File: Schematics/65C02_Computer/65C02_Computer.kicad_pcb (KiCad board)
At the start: 2 copper layers, 203.2 x 149.9 mm, 65 parts, among them J1 CLK Jumper, J10 LCD Connector, J2 Optional UART Port, J3 USB_B_Micro, J4 USB_B, J5 Power Connector, J6 Mini-DIN-6, J7 Expansion port, J8 VIA2PA, J9 VIA2PB, SW1 RESET, U1 74HC21, U10 ATtiny4313-PU, U11 65C22S, U12 65C22S, U2 74HC00, U3 74HC02, U4 NE555, U5 65C51N, U6 FT230XS, U7 65C02S, U8 28C256, U9 62256, X1 1MHz, X2 1.8432MHz

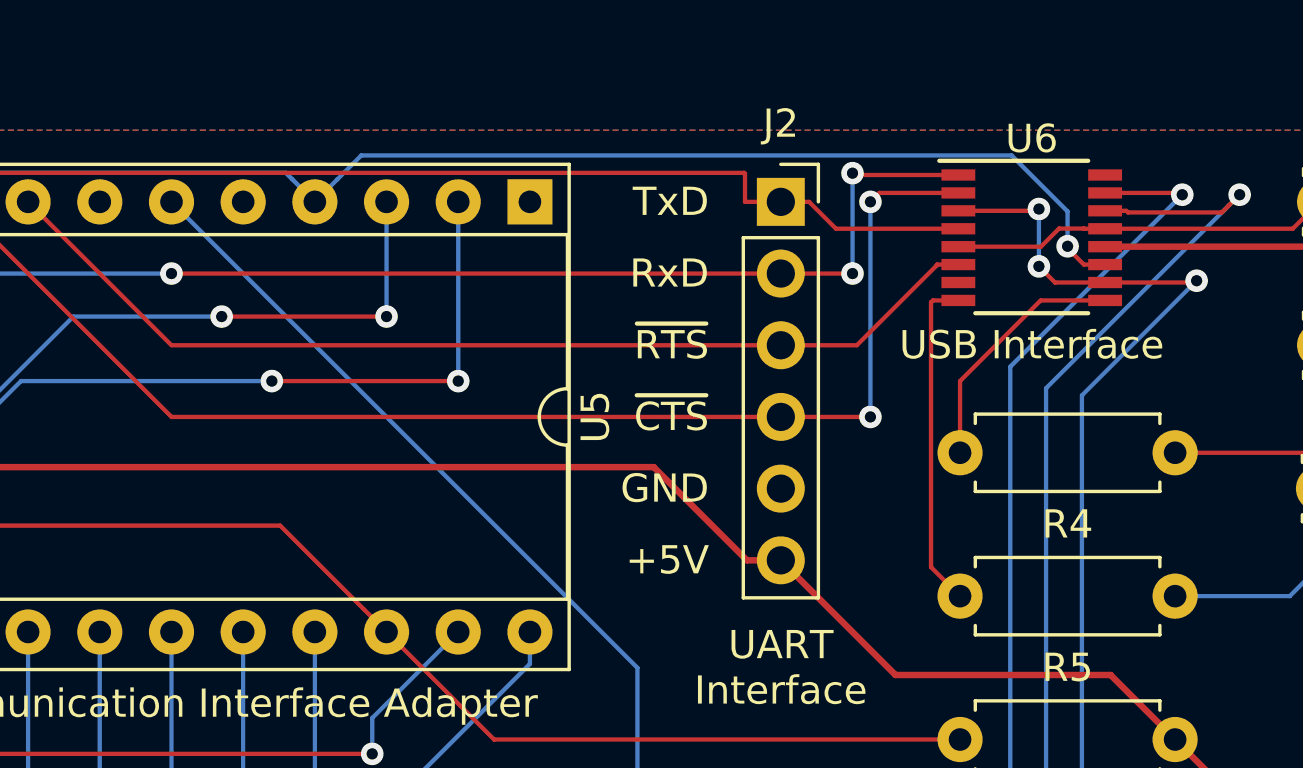
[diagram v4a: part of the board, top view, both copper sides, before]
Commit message: PCB RC4 - added longer pads to SSOP chip
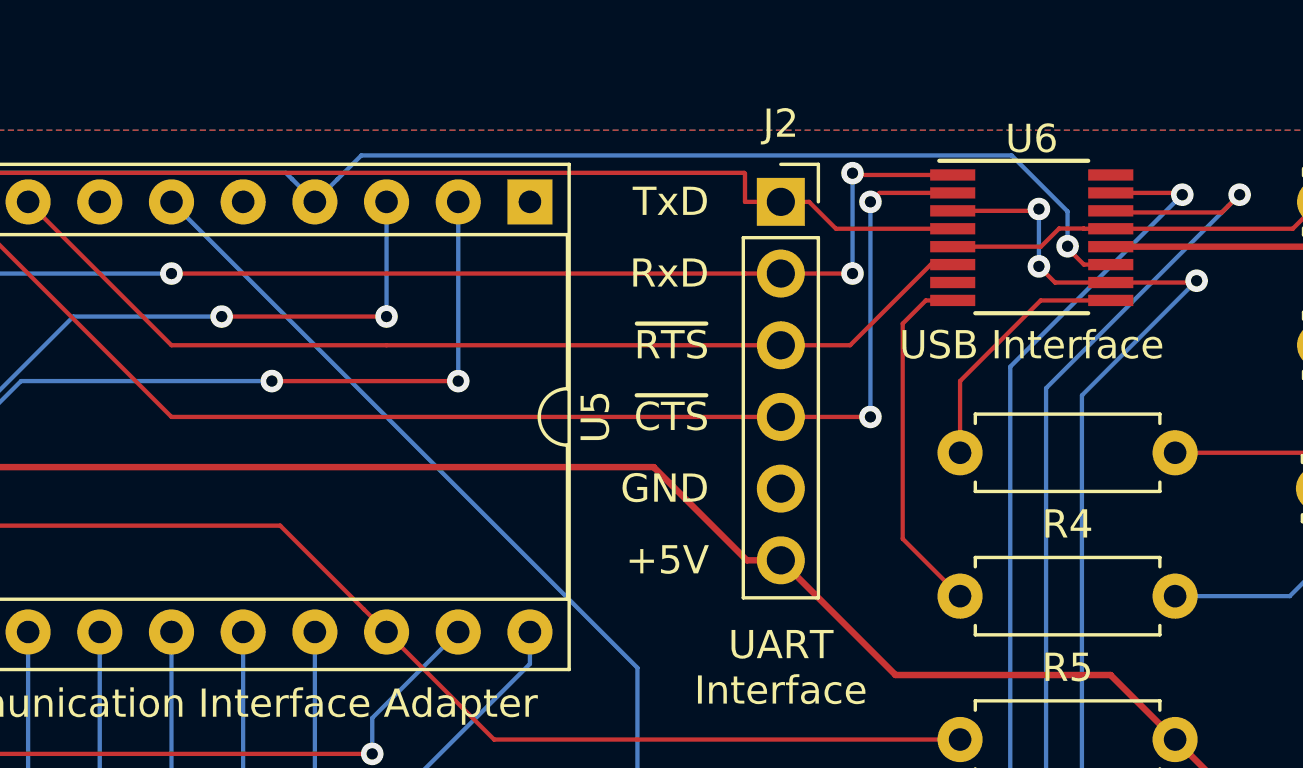
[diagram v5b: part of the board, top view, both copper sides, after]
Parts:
- U6: footprint Package_SO:SSOP-16_3.9x4.9mm_P0.635mm -> 65C02_Computer:SSOP-16_3.9x4.9mm_P0.635mm_long_pads
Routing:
- net USBD+: track 11.9 -> 12.6 mm
- net ~RTS: track 36.3 -> 36.8 mm
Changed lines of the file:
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@@
-(kicad_pcb (version 20171130) (host pcbnew "(5.1.5)-3")
+(kicad_pcb (version 20171130) (host pcbnew "(5.1.5-0-10_14)")
   (general
     (thickness 1.6)
     (drawings 126)
-    (tracks 1583)
+    (tracks 1585)
     (zones 0)
     (modules 65)
@@
     (0 F.Cu signal)
     (31 B.Cu signal)
-    (32 B.Adhes user)
-    (33 F.Adhes user)
-    (34 B.Paste user)
-    (35 F.Paste user)
+    (32 B.Adhes user hide)
+    (33 F.Adhes user hide)
+    (34 B.Paste user hide)
+    (35 F.Paste user hide)
     (36 B.SilkS user)
     (37 F.SilkS user)
     (38 B.Mask user)
     (39 F.Mask user)
-    (40 Dwgs.User user)
-    (41 Cmts.User user)
-    (42 Eco1.User user)
-    (43 Eco2.User user)
+    (40 Dwgs.User user hide)
+    (41 Cmts.User user hide)
+    (42 Eco1.User user hide)
+    (43 Eco2.User user hide)
     (44 Edge.Cuts user)
-    (45 Margin user)
-    (46 B.CrtYd user)
-    (47 F.CrtYd user)
+    (45 Margin user hide)
+    (46 B.CrtYd user hide)
+    (47 F.CrtYd user hide)
     (48 B.Fab user hide)
     (49 F.Fab user hide)
@@
       (psa4output false)
       (plotreference true)
-      (plotvalue true)
+      (plotvalue false)
       (plotinvisibletext false)
       (padsonsilk false)
@@
     (add_net +5V)
   )
-  (module Package_SO:SSOP-16_3.9x4.9mm_P0.635mm (layer F.Cu)
+  (module 65C02_Computer:SSOP-16_3.9x4.9mm_P0.635mm_long_pads (layer F.Cu)
     (at 189.23 29.21)
     (descr "SSOP16: plastic shrink small outline package; 16 leads; body width 3.9 mm; lead pitch 0.635; (see NXP SSOP-TSSOP-VSO-REFLOW.pdf and sot519-1_po.pdf)")
@@
     (fp_line (start -3.275 -2.725) (end 2 -2.725) (layer F.SilkS) (width 0.15))
     (fp_line (start -2 2.675) (end 2 2.675) (layer F.SilkS) (width 0.15))
-    (fp_line (start -3.45 2.8) (end 3.45 2.8) (layer F.CrtYd) (width 0.05))
-    (fp_line (start -3.45 -2.85) (end 3.45 -2.85) (layer F.CrtYd) (width 0.05))
-    (fp_line (start 3.45 -2.85) (end 3.45 2.8) (layer F.CrtYd) (width 0.05))
-    (fp_line (start -3.45 -2.85) (end -3.45 2.8) (layer F.CrtYd) (width 0.05))
+    (fp_line (start -3.65 2.8) (end 3.65 2.8) (layer F.CrtYd) (width 0.05))
+    (fp_line (start -3.65 -2.85) (end 3.65 -2.85) (layer F.CrtYd) (width 0.05))
+    (fp_line (start 3.65 -2.85) (end 3.65 2.8) (layer F.CrtYd) (width 0.05))
+    (fp_line (start -3.65 -2.85) (end -3.65 2.8) (layer F.CrtYd) (width 0.05))
     (fp_line (start -1.95 -1.45) (end -0.95 -2.45) (layer F.Fab) (width 0.15))
     (fp_line (start -1.95 2.45) (end -1.95 -1.45) (layer F.Fab) (width 0.15))
@@
     (fp_line (start 1.95 -2.45) (end 1.95 2.45) (layer F.Fab) (width 0.15))
     (fp_line (start -0.95 -2.45) (end 1.95 -2.45) (layer F.Fab) (width 0.15))
-    (pad 16 smd rect (at 2.6 -2.2225) (size 1.2 0.4) (layers F.Cu F.Paste F.Mask)
+    (pad 16 smd rect (at 2.8 -2.2225) (size 1.6 0.4) (layers F.Cu F.Paste F.Mask)
       (net 105 "Net-(U6-Pad16)"))
-    (pad 15 smd rect (at 2.6 -1.5875) (size 1.2 0.4) (layers F.Cu F.Paste F.Mask)
+    (pad 15 smd rect (at 2.8 -1.5875) (size 1.6 0.4) (layers F.Cu F.Paste F.Mask)
       (net 4 "Net-(D2-Pad1)"))
-    (pad 14 smd rect (at 2.6 -0.9525) (size 1.2 0.4) (layers F.Cu F.Paste F.Mask)
+    (pad 14 smd rect (at 2.8 -0.9525) (size 1.6 0.4) (layers F.Cu F.Paste F.Mask)
       (net 7 "Net-(D3-Pad1)"))
-    (pad 13 smd rect (at 2.6 -0.3175) (size 1.2 0.4) (layers F.Cu F.Paste F.Mask)
+    (pad 13 smd rect (at 2.8 -0.3175) (size 1.6 0.4) (layers F.Cu F.Paste F.Mask)
       (net 2 GND))
-    (pad 12 smd rect (at 2.6 0.3175) (size 1.2 0.4) (layers F.Cu F.Paste F.Mask)
+    (pad 12 smd rect (at 2.8 0.3175) (size 1.6 0.4) (layers F.Cu F.Paste F.Mask)
       (net 1 +5V))
-    (pad 11 smd rect (at 2.6 0.9525) (size 1.2 0.4) (layers F.Cu F.Paste F.Mask)
+    (pad 11 smd rect (at 2.8 0.9525) (size 1.6 0.4) (layers F.Cu F.Paste F.Mask)
       (net 37 ~RES))
-    (pad 10 smd rect (at 2.6 1.5875) (size 1.2 0.4) (layers F.Cu F.Paste F.Mask)
+    (pad 10 smd rect (at 2.8 1.5875) (size 1.6 0.4) (layers F.Cu F.Paste F.Mask)
       (net 72 "Net-(R10-Pad1)"))
-    (pad 9 smd rect (at 2.6 2.2225) (size 1.2 0.4) (layers F.Cu F.Paste F.Mask)
+    (pad 9 smd rect (at 2.8 2.2225) (size 1.6 0.4) (layers F.Cu F.Paste F.Mask)
       (net 71 USBD-))
-    (pad 8 smd rect (at -2.6 2.2225) (size 1.2 0.4) (layers F.Cu F.Paste F.Mask)
+    (pad 8 smd rect (at -2.8 2.2225) (size 1.6 0.4) (layers F.Cu F.Paste F.Mask)
       (net 70 USBD+))
-    (pad 7 smd rect (at -2.6 1.5875) (size 1.2 0.4) (layers F.Cu F.Paste F.Mask)
+    (pad 7 smd rect (at -2.8 1.5875) (size 1.6 0.4) (layers F.Cu F.Paste F.Mask)
       (net 106 "Net-(U6-Pad7)"))
-    (pad 6 smd rect (at -2.6 0.9525) (size 1.2 0.4) (layers F.Cu F.Paste F.Mask)
+    (pad 6 smd rect (at -2.8 0.9525) (size 1.6 0.4) (layers F.Cu F.Paste F.Mask)
       (net 93 ~RTS))
-    (pad 5 smd rect (at -2.6 0.3175) (size 1.2 0.4) (layers F.Cu F.Paste F.Mask)
+    (pad 5 smd rect (at -2.8 0.3175) (size 1.6 0.4) (layers F.Cu F.Paste F.Mask)
       (net 2 GND))
-    (pad 4 smd rect (at -2.6 -0.3175) (size 1.2 0.4) (layers F.Cu F.Paste F.Mask)
+    (pad 4 smd rect (at -2.8 -0.3175) (size 1.6 0.4) (layers F.Cu F.Paste F.Mask)
       (net 92 TxD))
-    (pad 3 smd rect (at -2.6 -0.9525) (size 1.2 0.4) (layers F.Cu F.Paste F.Mask)
+    (pad 3 smd rect (at -2.8 -0.9525) (size 1.6 0.4) (layers F.Cu F.Paste F.Mask)
       (net 72 "Net-(R10-Pad1)"))
-    (pad 2 smd rect (at -2.6 -1.5875) (size 1.2 0.4) (layers F.Cu F.Paste F.Mask)
+    (pad 2 smd rect (at -2.8 -1.5875) (size 1.6 0.4) (layers F.Cu F.Paste F.Mask)
       (net 91 ~CTS))
-    (pad 1 smd rect (at -2.6 -2.2225) (size 1.2 0.4) (layers F.Cu F.Paste F.Mask)
+    (pad 1 smd rect (at -2.8 -2.2225) (size 1.6 0.4) (layers F.Cu F.Paste F.Mask)
       (net 90 RxD))
     (model ${KISYS3DMOD}/Package_SO.3dshapes/SSOP-16_3.9x4.9mm_P0.635mm.wrl
@@
   (segment (start 196.075399 80.251399) (end 198.092601 82.268601) (width 0.1524) (layer F.Cu) (net 69))
   (segment (start 187.96 81.28) (end 188.988601 80.251399) (width 0.1524) (layer F.Cu) (net 69) (status 10))
-  (segment (start 185.661399 31.501201) (end 185.6776 31.485) (width 0.1524) (layer F.Cu) (net 70))
-  (segment (start 185.661399 40.881399) (end 185.661399 31.501201) (width 0.1524) (layer F.Cu) (net 70))
-  (segment (start 186.69 41.91) (end 185.661399 40.881399) (width 0.1524) (layer F.Cu) (net 70))
-  (segment (start 185.7301 31.4325) (end 186.63 31.4325) (width 0.1524) (layer F.Cu) (net 70))
-  (segment (start 185.661399 31.501201) (end 185.7301 31.4325) (width 0.1524) (layer F.Cu) (net 70))
+  (segment (start 185.4776 31.4325) (end 186.43 31.4325) (width 0.1524) (layer F.Cu) (net 70))
+  (segment (start 184.658 39.878) (end 184.658 32.2521) (width 0.1524) (layer F.Cu) (net 70))
+  (segment (start 184.658 32.2521) (end 185.4776 31.4325) (width 0.1524) (layer F.Cu) (net 70))
+  (segment (start 186.69 41.91) (end 184.658 39.878) (width 0.1524) (layer F.Cu) (net 70))
   (segment (start 189.5475 31.4325) (end 191.83 31.4325) (width 0.1524) (layer F.Cu) (net 71))
   (segment (start 186.69 36.83) (end 186.69 34.29) (width 0.1524) (layer F.Cu) (net 71))
@@
   (segment (start 185.8776 30.1625) (end 186.63 30.1625) (width 0.1524) (layer F.Cu) (net 93))
   (segment (start 153.67 27.94) (end 158.75 33.02) (width 0.1524) (layer F.Cu) (net 93))
-  (segment (start 158.75 33.02) (end 183.033518 33.02) (width 0.1524) (layer F.Cu) (net 93))
-  (segment (start 183.033518 33.02) (end 185.868518 30.185) (width 0.1524) (layer F.Cu) (net 93))
   (segment (start 185.868518 30.171582) (end 185.8776 30.1625) (width 0.1524) (layer F.Cu) (net 93))
   (segment (start 185.868518 30.185) (end 185.868518 30.171582) (width 0.1524) (layer F.Cu) (net 93))
+  (segment (start 166.37 33.02) (end 180.34 33.02) (width 0.1524) (layer F.Cu) (net 93))
+  (segment (start 158.75 33.02) (end 166.37 33.02) (width 0.1524) (layer F.Cu) (net 93))
+  (segment (start 185.653518 30.1625) (end 186.43 30.1625) (width 0.1524) (layer F.Cu) (net 93))
+  (segment (start 182.796018 33.02) (end 185.653518 30.1625) (width 0.1524) (layer F.Cu) (net 93))
+  (segment (start 180.34 33.02) (end 182.796018 33.02) (width 0.1524) (layer F.Cu) (net 93))
   (segment (start 175.26 62.484) (end 171.958 65.786) (width 0.1524) (layer B.Cu) (net 94))
   (via (at 171.958 78.74) (size 0.8) (drill 0.4) (layers F.Cu B.Cu) (net 94))
